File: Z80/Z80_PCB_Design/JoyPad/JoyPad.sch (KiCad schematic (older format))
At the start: 22 parts, among them J1 Conn_01x12, SW1 SW_Push, SW2 SW_Push, SW3 SW_Push, SW4 SW_Push, SW5 SW_Push, SW6 SW_Push, SW7 SW_Push, SW8 SW_Push

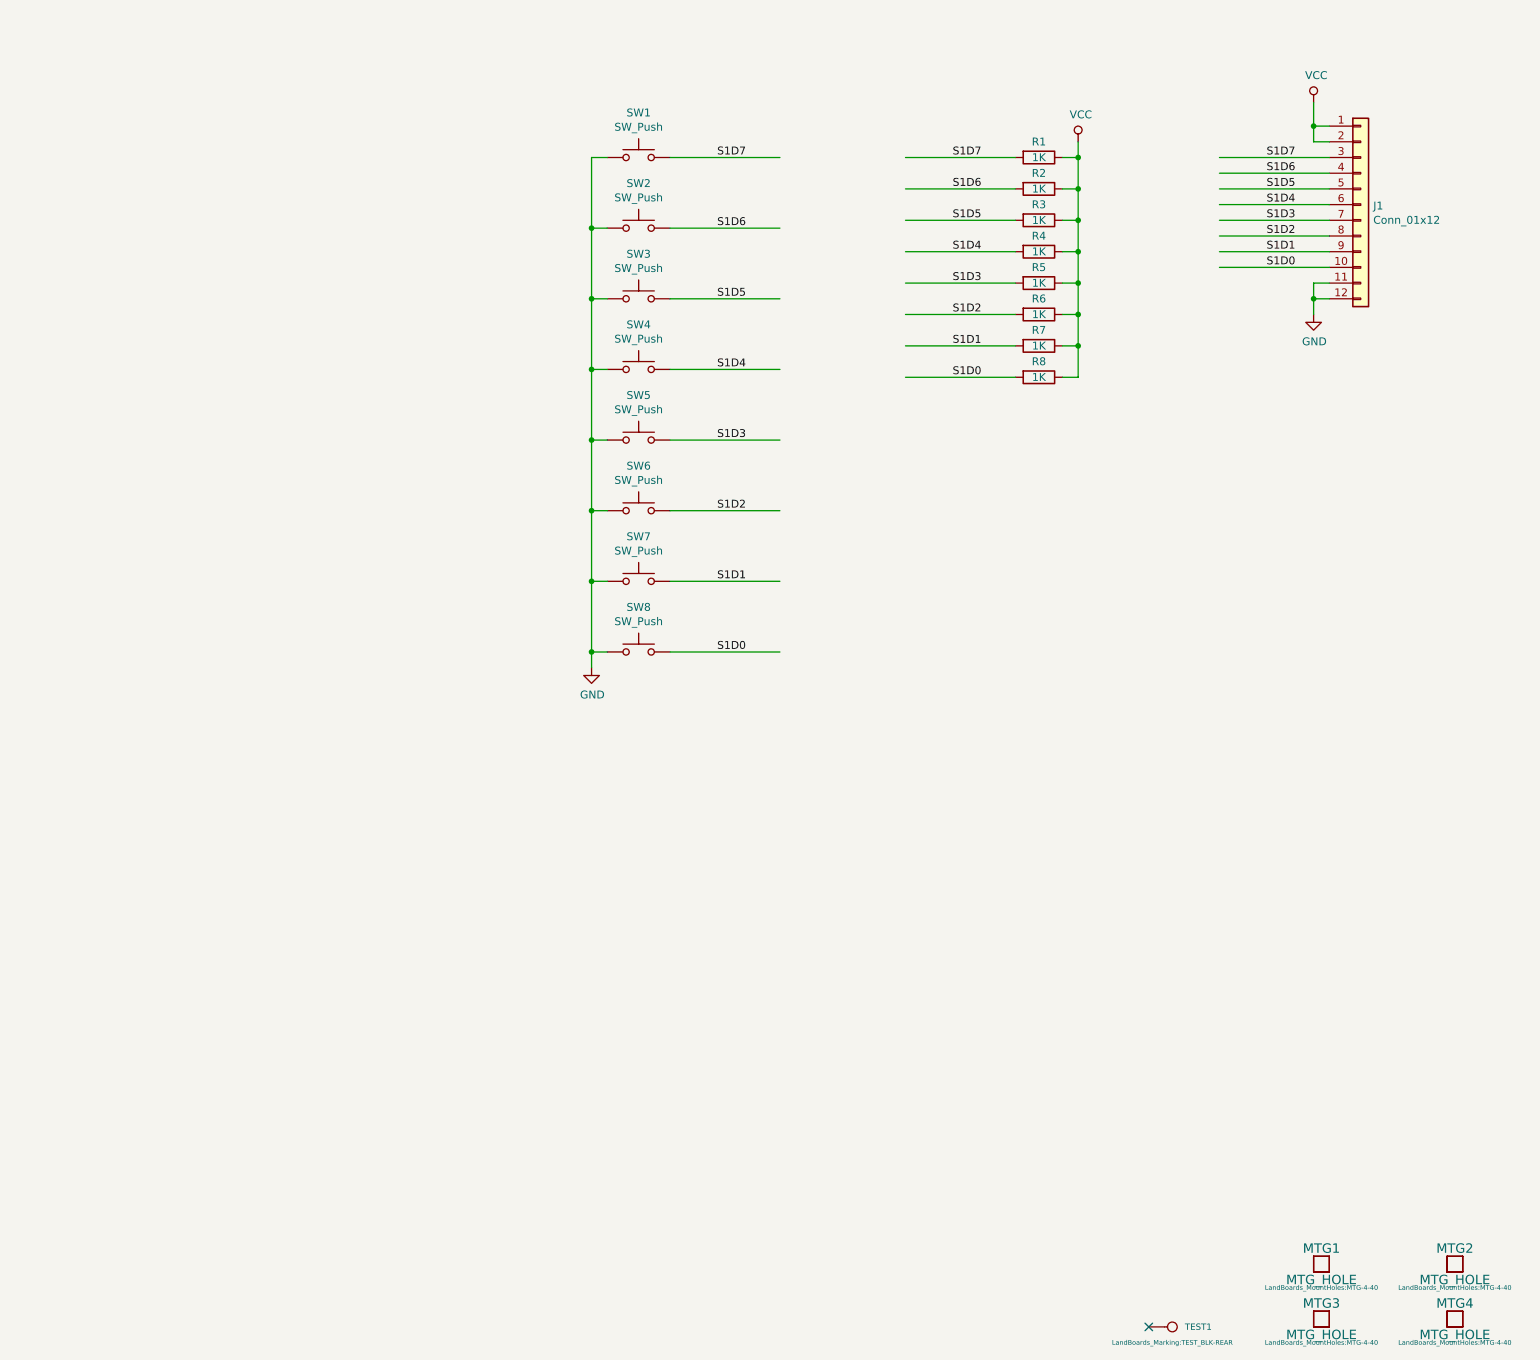
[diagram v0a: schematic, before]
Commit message: Front panel toggle on LED release
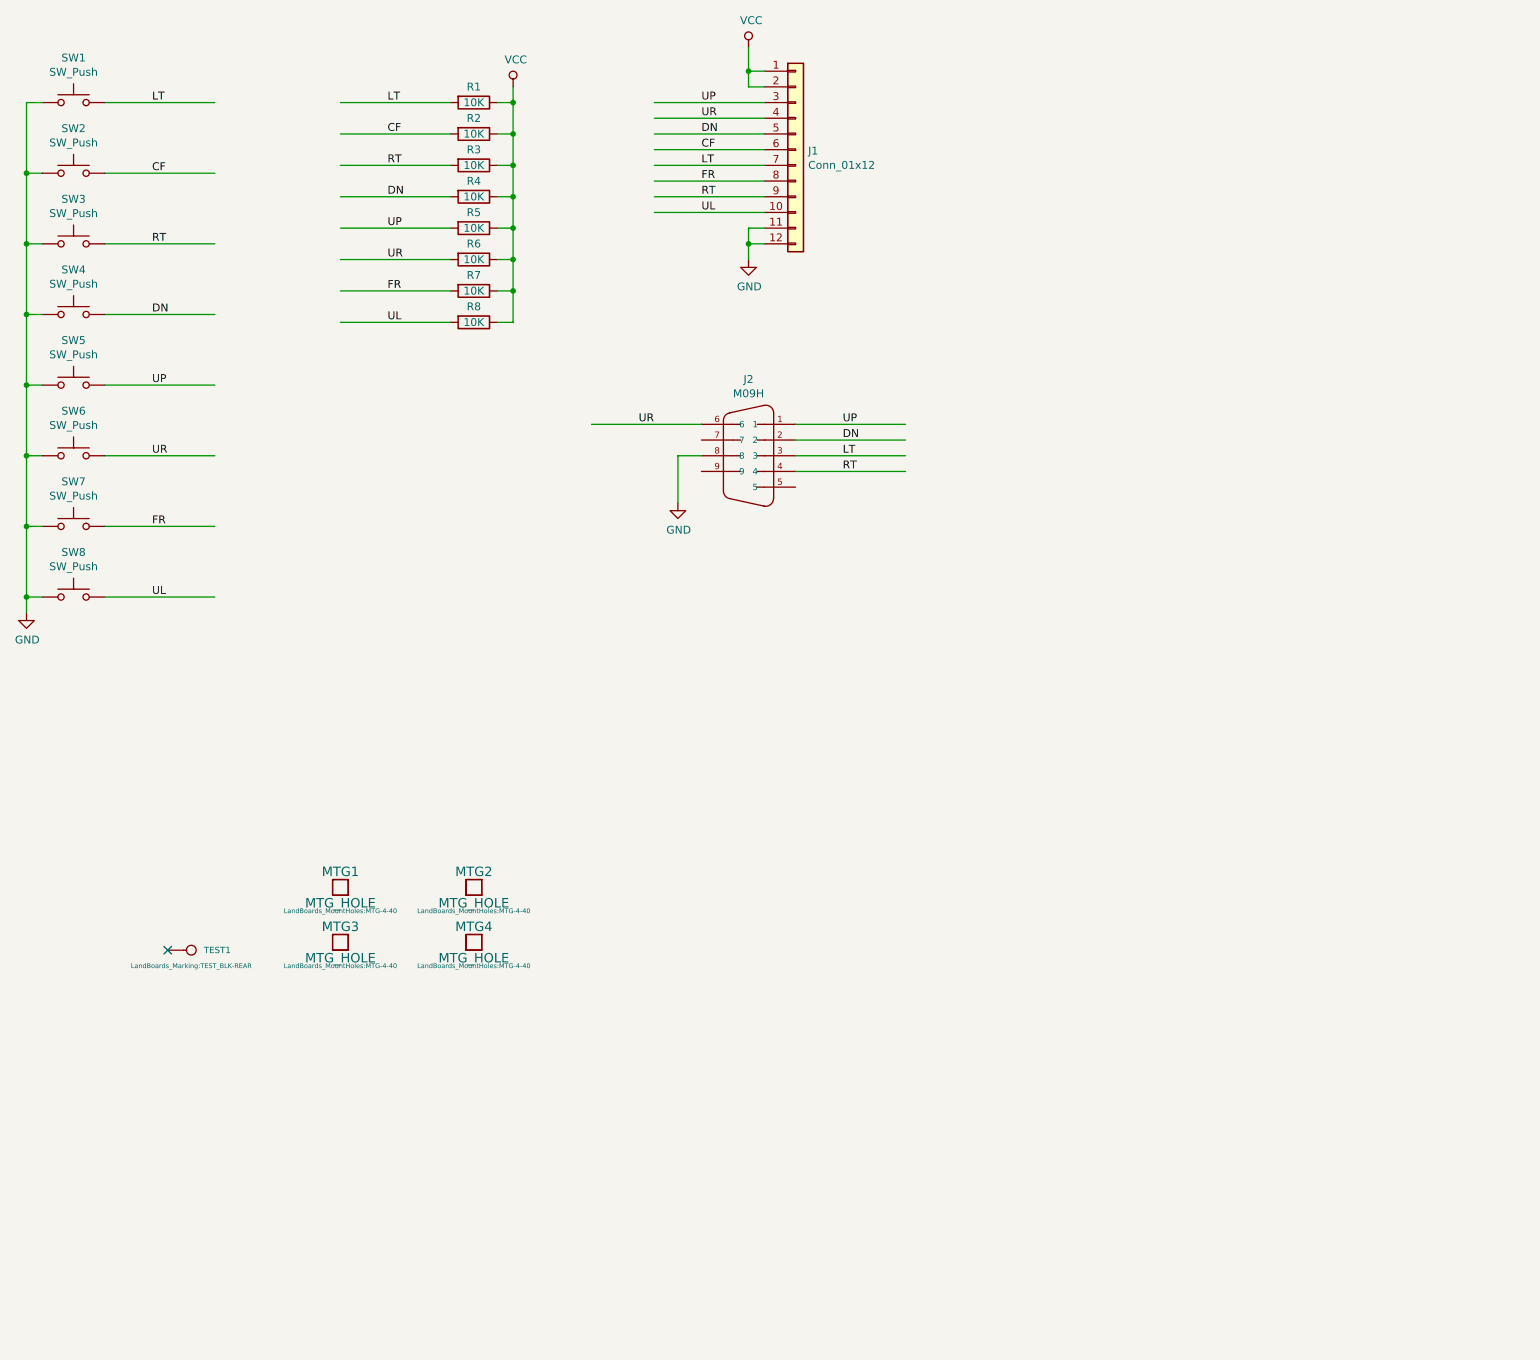
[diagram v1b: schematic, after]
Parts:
- added J2: M09H, Connector_Dsub:DSUB-9_Male_Horizontal_P2.77x2.84mm_EdgePinOffset4.94mm_Housed_MountingHolesOffset7.48mm, symbol con-subd:M09H
- J1: footprint Connector_PinSocket_2.54mm:PinSocket_2x06_P2.54mm_Horizontal -> Connector_PinHeader_2.54mm:PinHeader_1x12_P2.54mm_Vertical
- R1, R2, R3, R4, R5, R6, R7, R8: value 1K -> 10K
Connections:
- net labels added: CF, DN, FR, LT, RT, UL, UP, UR
- net labels removed: S1D0, S1D1, S1D2, S1D3, S1D4, S1D5, S1D6, S1D7
- wire segments 64 -> 71
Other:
- moved on the sheet: J1, MTG1, MTG2, MTG3, MTG4, R1, R2, R3, R4, R5, R6, R7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
